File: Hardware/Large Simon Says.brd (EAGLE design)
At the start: 59.7 x 53.3 mm, 25 parts, among them Q1 2N3904, Q2 2N3904, Q3 2N3904, Q4 2N3904, U1 ARDUINO_SHIELD, U2 AUDIO-AMP

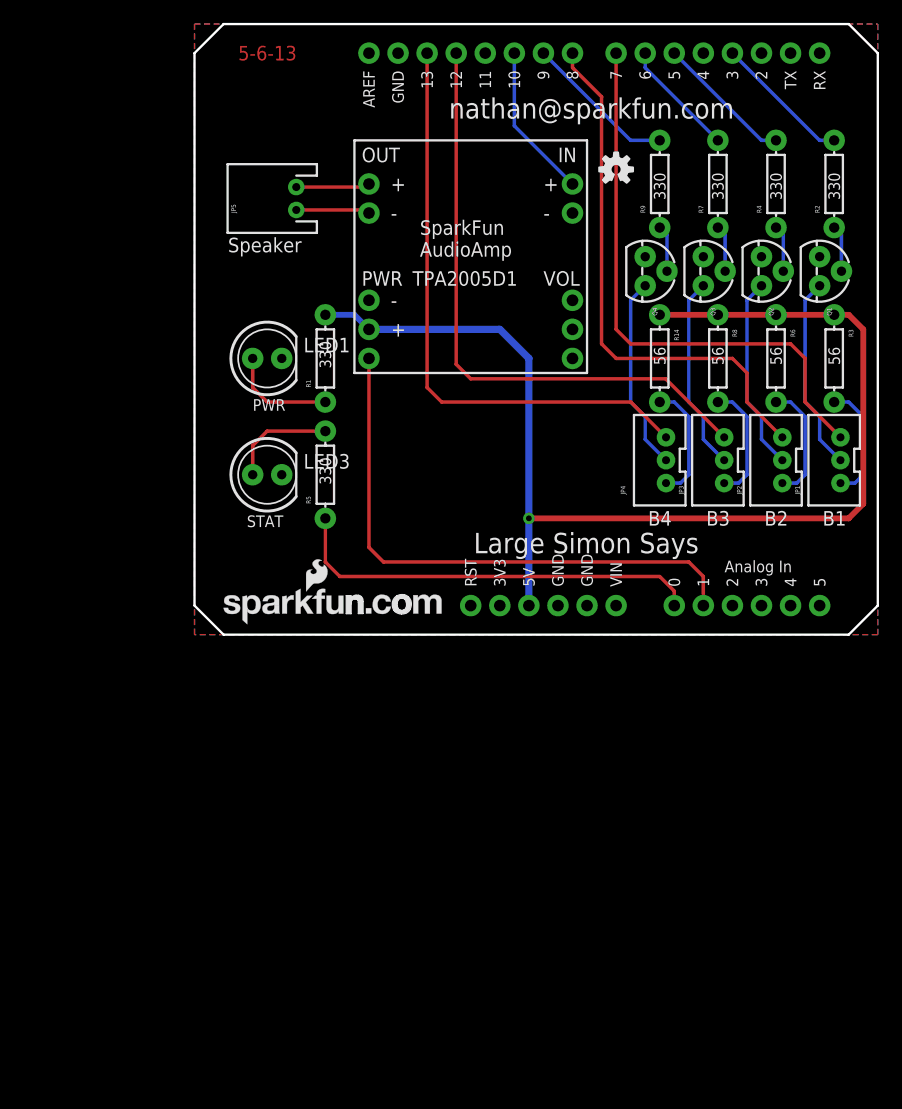
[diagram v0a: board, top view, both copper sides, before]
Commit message: Adding firmware. Small changes to hardware.
The button connectors are missing a ground connection. Thought I could
do it with three, but it was a mistake.
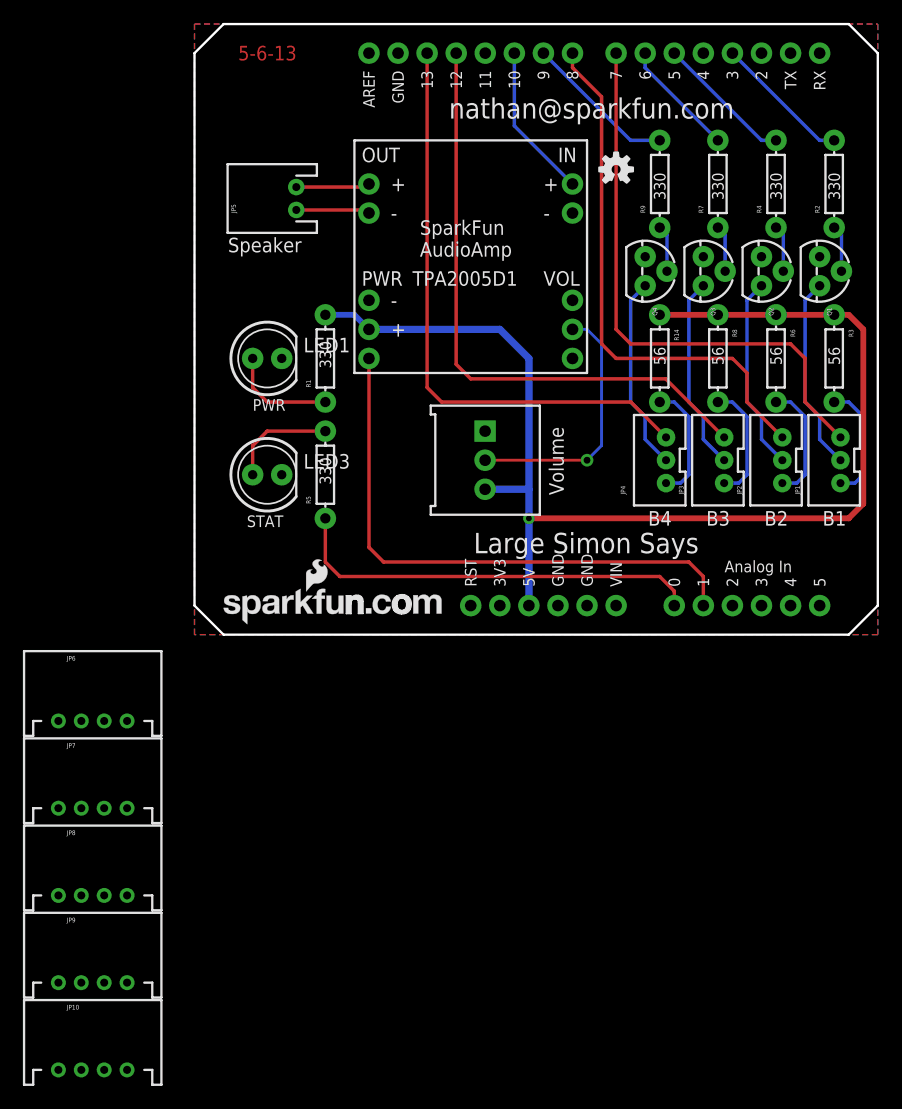
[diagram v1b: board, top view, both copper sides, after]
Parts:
- added JP10, JP6, JP7, JP8, JP9: (no value), SparkFun-Connectors:JST-4-PTH
- added R10: Vol Control, SparkFun-Electromechanical:3386U
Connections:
- new net N$14: R10.2, U2.VOL
- net GND: now also R10.1
- net VCC: now also R10.3
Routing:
- net N$14: track 0.00 -> 22.7 mm, vias 0 -> 1
- net VCC: track 104.2 -> 108.1 mm
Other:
- board text added: "Volume"
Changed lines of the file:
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@@
 <layer number="106" name="bPlate" color="7" fill="1" visible="no" active="yes"/>
 <layer number="107" name="Crop" color="7" fill="1" visible="no" active="yes"/>
-<layer number="108" name="tplace-old" color="10" fill="1" visible="yes" active="yes"/>
-<layer number="109" name="ref-old" color="11" fill="1" visible="yes" active="yes"/>
+<layer number="108" name="tplace-old" color="10" fill="1" visible="no" active="yes"/>
+<layer number="109" name="ref-old" color="11" fill="1" visible="no" active="yes"/>
 <layer number="116" name="Patch_BOT" color="9" fill="4" visible="no" active="yes"/>
 <layer number="121" name="_tsilk" color="7" fill="1" visible="no" active="yes"/>
@@
 <text x="2.921" y="33.401" size="1.27" layer="21" font="vector" ratio="15">Speaker</text>
 <text x="3.81" y="50.165" size="1.27" layer="1" font="vector" ratio="25">5-6-13</text>
+<text x="32.258" y="12.192" size="1.27" layer="21" font="vector" ratio="15" rot="R90">Volume</text>
 </plain>
 <attributes>
@@
 <element name="U2" library="SparkFun-Boards" package="AUDIO-AMP-MONO" value="AUDIO-AMP" x="24.13" y="33.02"/>
 <element name="JP5" library="SparkFun-Connectors" package="JST-2-PTH" value="Speaker" x="8.89" y="38.1" rot="R90"/>
+<element name="R10" library="SparkFun-Electromechanical" package="3386U" value="Vol Control" x="25.4" y="15.24" rot="R270"/>
+<element name="JP6" library="SparkFun-Connectors" package="JST-4-PTH" value="" x="-8.89" y="-2.54"/>
+<element name="JP7" library="SparkFun-Connectors" package="JST-4-PTH" value="" x="-8.89" y="-10.16"/>
+<element name="JP8" library="SparkFun-Connectors" package="JST-4-PTH" value="" x="-8.89" y="-17.78"/>
+<element name="JP9" library="SparkFun-Connectors" package="JST-4-PTH" value="" x="-8.89" y="-25.4"/>
+<element name="JP10" library="SparkFun-Connectors" package="JST-4-PTH" value="" x="-8.89" y="-33.02"/>
 </elements>
 <signals>
@@
 <contactref element="U2" pad="IN-"/>
 <contactref element="U2" pad="VOL-"/>
+<contactref element="R10" pad="1"/>
 </signal>
 <signal name="VCC" class="1">
@@
 <contactref element="U2" pad="PWR+"/>
 <wire x1="29.21" y1="2.54" x2="29.21" y2="10.16" width="0.635" layer="16"/>
-<wire x1="29.21" y1="10.16" x2="29.21" y2="24.13" width="0.635" layer="16"/>
+<wire x1="29.21" y1="10.16" x2="29.21" y2="12.7" width="0.635" layer="16"/>
+<wire x1="29.21" y1="12.7" x2="29.21" y2="24.13" width="0.635" layer="16"/>
 <wire x1="29.21" y1="24.13" x2="26.67" y2="26.67" width="0.635" layer="16"/>
 <wire x1="26.67" y1="26.67" x2="15.24" y2="26.67" width="0.635" layer="16"/>
@@
 <wire x1="15.24" y1="26.67" x2="13.97" y2="27.94" width="0.508" layer="16"/>
 <wire x1="13.97" y1="27.94" x2="11.43" y2="27.94" width="0.508" layer="16"/>
+<contactref element="R10" pad="3"/>
+<wire x1="25.385" y1="12.7" x2="29.21" y2="12.7" width="0.635" layer="16"/>
 </signal>
 <signal name="N$1">
@@
 <wire x1="14.97" y1="37.1" x2="15.24" y2="36.83" width="0.3048" layer="1"/>
 </signal>
+<signal name="N$14">
+<contactref element="U2" pad="VOL"/>
+<contactref element="R10" pad="2"/>
+<via x="34.29" y="15.24" extent="1-16" drill="0.6"/>
+<wire x1="34.29" y1="15.24" x2="25.385" y2="15.24" width="0.254" layer="1"/>
+<wire x1="33.02" y1="26.67" x2="34.29" y2="26.67" width="0.254" layer="16"/>
+<wire x1="34.29" y1="26.67" x2="35.56" y2="25.4" width="0.254" layer="16"/>
+<wire x1="35.56" y1="25.4" x2="35.56" y2="16.51" width="0.254" layer="16"/>
+<wire x1="35.56" y1="16.51" x2="34.29" y2="15.24" width="0.254" layer="16"/>
+</signal>
 </signals>
